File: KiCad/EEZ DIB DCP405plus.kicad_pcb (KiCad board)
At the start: 4 copper layers, 180 x 103.5 mm, 427 parts, among them IC1 ADS131A04IPBSR, IC10 TC77-5.0MCTTR, IC11 REF5025AIDR, IC12 MC79L05, IC13 MC78L05, IC14 PCAL9722HNMP, IC15 TPS7A2033PDBVR, IC16 LM5145RGYR, IC17 LTC2050HVCS8#PBF, IC18 TL072D, IC19 TL072D, IC2 ISO6762FDWR, IC20 SN74LVC1G3157DCKR, IC21 SN74LVC2G08DCTR, IC22 LM293D, IC23 OPA376AIDBVR, IC24 SN74LVC1G3157DCKR, IC25 SN74LVC1G3157DCKR, IC26 LM293D, IC27 MAX9141ESA, IC3 ISO6762FDWR, IC4 ISO6520DR, IC5 STM32H503CBT6, IC6 M24C32-DFDW6TP, IC7 DAC8552IDGKR, IC8 74AUP1G74DC,125, IC9 TPS54060DGQ, J1 572-0500, J2 572-0100, K1 FTR-C1GA012G-B05 or EE2-12NU-L, Q10 MMBT5401, Q11 MMBT5401, Q12 BCP56-16.115, Q13 MMBT5551, Q14 IRFP250NPBF, Q15 BCP56-16.115, Q16 BC857C, Q17 IRFI9Z34GPBF, Q18 PSMN0R9-25YLC, Q19 PSMN0R9-25YLC, Q20 MMBT5551, Q21 MMBT5551, Q22 MMBT5551, Q23 MMBT5401, Q24 2N7002, Q25 2N7002, Q26 2N7002, Q27 2N7002, Q28 MMBT5551, Q29 FMMT493TA, Q3 BSS84, Q30 BT139B-600E, Q31 PSMN013-60YL, Q4 BSC117N08NS5ATMA1, Q5 BSC039N06NSATMA1, Q6 2N7002, Q7 MMBT5401, Q8 SQJ457EP-T1_BE3, Q9 MMBT5551, X1 PCB Edge connector, X2 N.C., X3 B4PS-VH (LF)(SN), X4 TBP03R1-350-03BE, X5 ZL263-20DG, Y1 ECS-163.84-10-33-JGN-TR, Y2 ABM8-25.000MHZ-D2X-T

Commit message: #6
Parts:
- moved R7 1.53 mm to (172.1, 98.2)
- moved R5 1.49 mm to (172.1, 104.5)
- moved R6 1.46 mm to (172.1, 103.0)
- moved R8 1.40 mm to (172.1, 96.7)
- turned C3 to -90 degrees
- turned C4 to -90 degrees
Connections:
- IC1 pad 3: /DIB isolators, EEPROM, ADC, MCU/I_MON_AIN -> /DIB isolators, EEPROM, ADC, MCU/I_MON_AIN-
- IC1 pad 4: /DIB isolators, EEPROM, ADC, MCU/I_MON_AIN- -> /DIB isolators, EEPROM, ADC, MCU/I_MON_AIN
- IC1 pad 7: /DIB isolators, EEPROM, ADC, MCU/I_SET_AIN -> /DIB isolators, EEPROM, ADC, MCU/I_SET_AIN-
- IC1 pad 8: /DIB isolators, EEPROM, ADC, MCU/I_SET_AIN- -> /DIB isolators, EEPROM, ADC, MCU/I_SET_AIN
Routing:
- net PREG_OUT-: track 223.5 -> 221.4 mm
- net GND: track 111.9 -> 110.6 mm
- net /DIB isolators, EEPROM, ADC, MCU/I_SET_AIN: track 7.16 -> 8.28 mm
- net /DIB isolators, EEPROM, ADC, MCU/I_SET_AIN-: track 8.22 -> 7.17 mm
- net POST_OUT-: track 231.6 -> 232.5 mm
- net U_SET: track 123.4 -> 122.8 mm
- net I_SET: track 115.5 -> 116.1 mm
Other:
- board text added: "EEZ DCP405+ (04/2026 ${project_version})"
- board text removed: "EEZ DCP405+ (01/2026 ${project_version})"

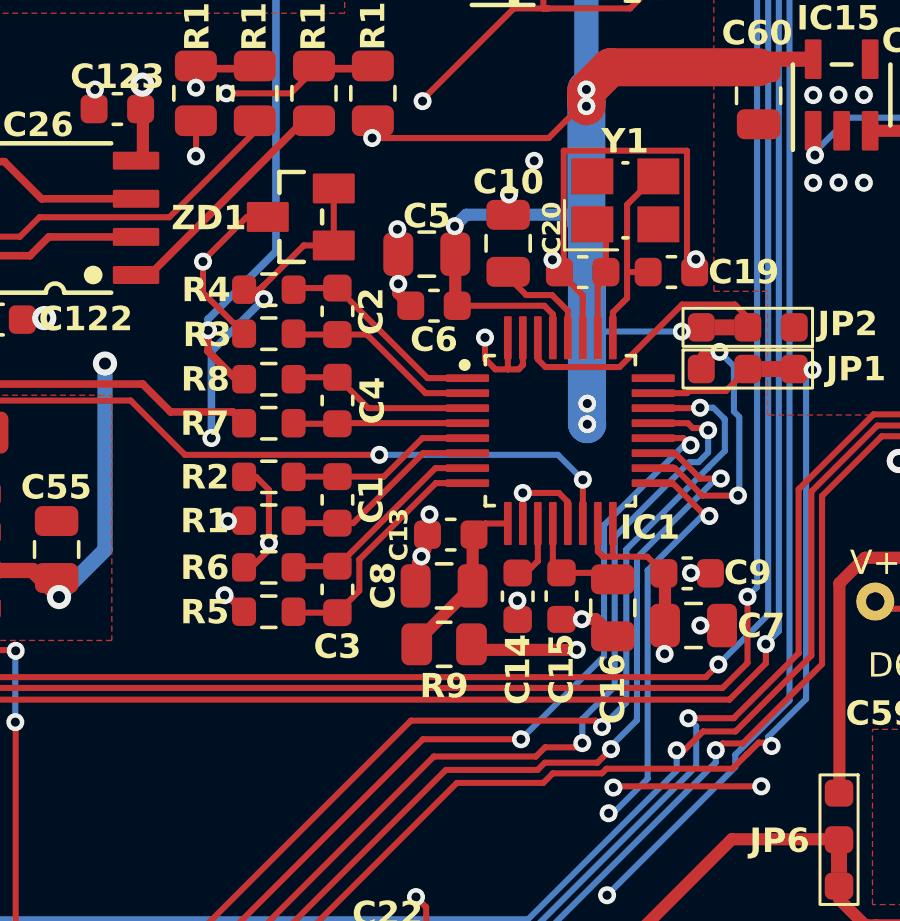
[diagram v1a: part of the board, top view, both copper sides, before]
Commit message: Silkscreen updated
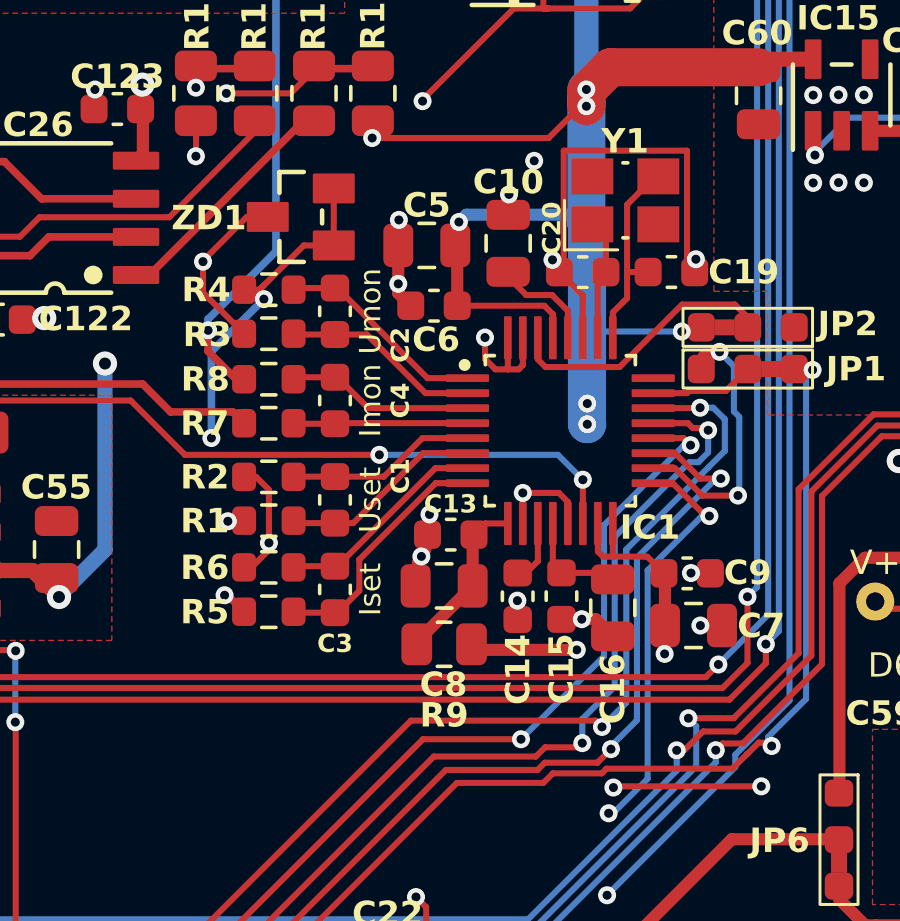
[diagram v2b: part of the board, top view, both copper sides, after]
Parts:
- moved C5 0.29 mm to (177.3, 92.3)
- moved C1 0.08 mm to (174.3, 100.8)
- moved C2 0.08 mm to (174.3, 94.5)
- moved C3 0.08 mm to (174.3, 103.7)
- moved C4 0.08 mm to (174.3, 97.4)
